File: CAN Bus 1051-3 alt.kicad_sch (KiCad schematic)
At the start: 12 parts, among them J1 Conn_01x05_Pin, J2 Conn_01x03_Pin, U1 TJA1051TK-3

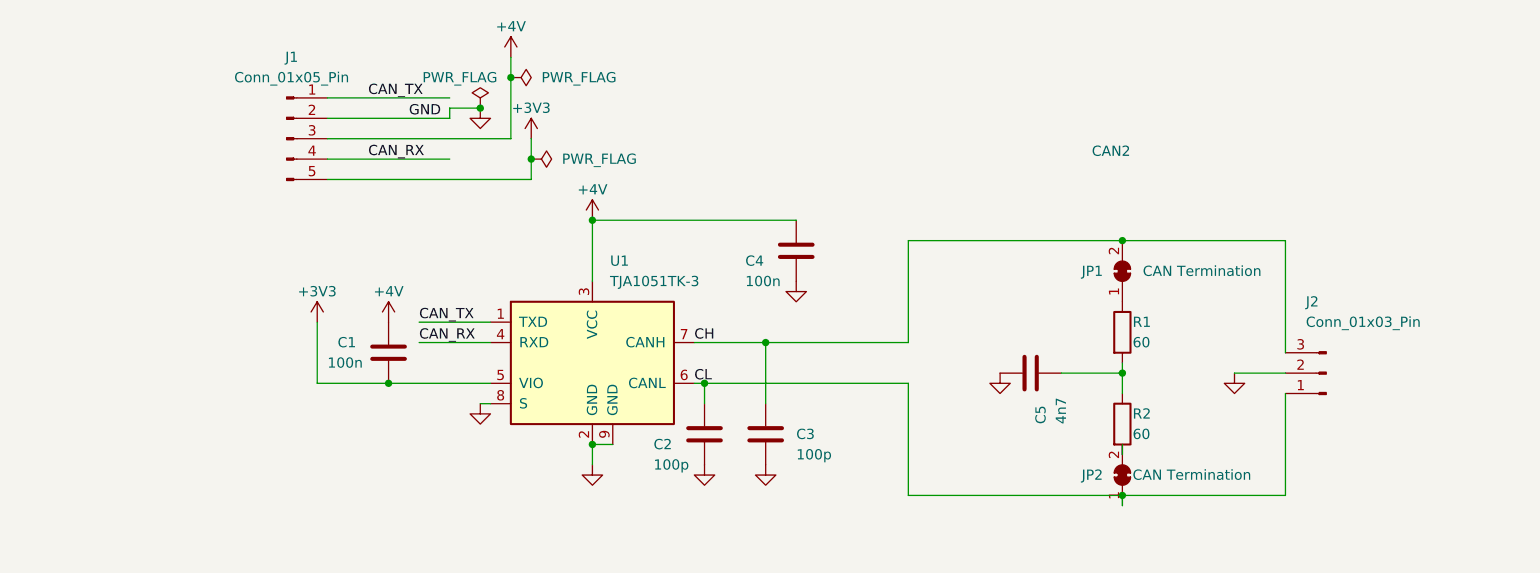
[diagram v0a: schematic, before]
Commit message: alternate layout that conserves more space
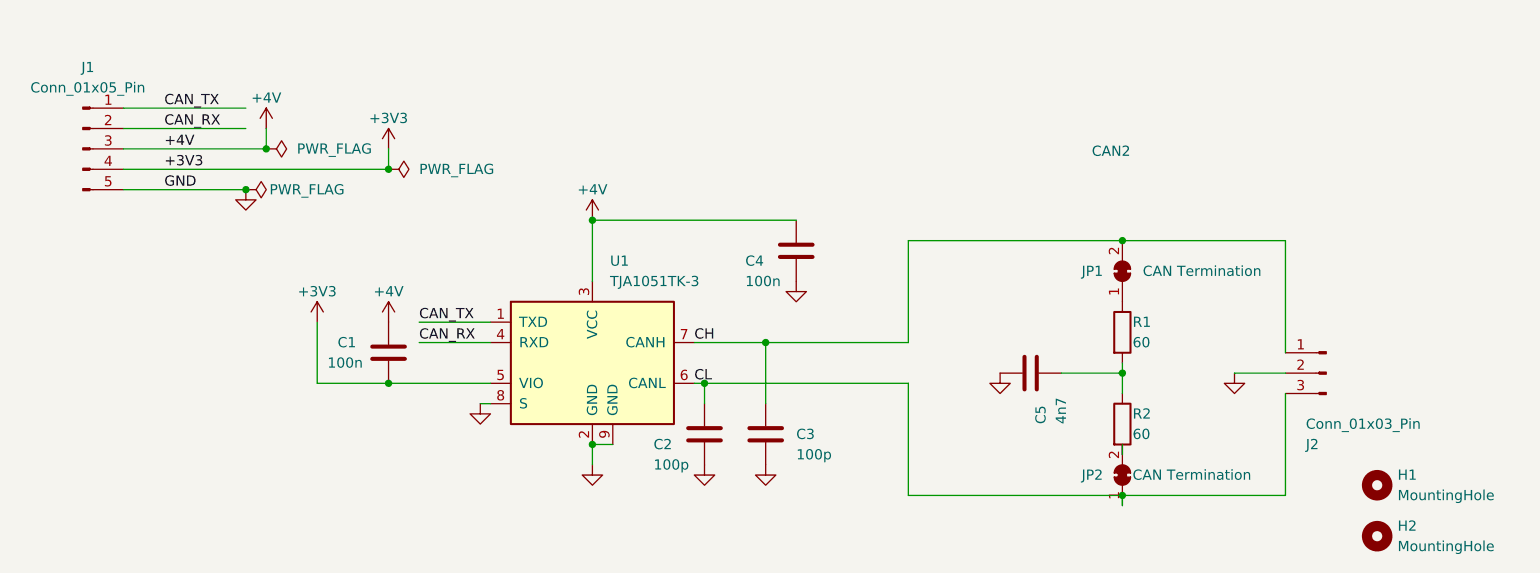
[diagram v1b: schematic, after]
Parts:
- added H1, H2: MountingHole, MountingHole:MountingHole_2.2mm_M2, symbol Mechanical:MountingHole
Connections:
- net +3V3: now also J1.4 (Pin_4); no longer J1.5 (Pin_5)
- net CAN_RX: now also J1.2 (Pin_2); no longer J1.4 (Pin_4)
- net CH: now also J2.1 (Pin_1); no longer J2.3 (Pin_3)
- net CL: now also J2.3 (Pin_3); no longer J2.1 (Pin_1)
- net GND: now also J1.5 (Pin_5); no longer J1.2 (Pin_2)
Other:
- moved on the sheet: J1, J2
